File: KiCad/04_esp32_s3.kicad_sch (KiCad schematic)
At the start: 32 parts, among them IC401 ESP32-S3-WROOM-1-N16R8, J401 Conn_01x04_Pin, J402 Conn_01x04_Pin, J403 Conn_01x04_Pin, J404 TF-01A, J405 Conn_01x08_Pin, Q401 SS8050, Q402 SS8050

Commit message: Fix DRC
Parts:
- removed J405: Conn_01x08_Pin, Connector_PinHeader_2.54mm:PinHeader_1x08_P2.54mm_Vertical, symbol Connector:Conn_01x08_Pin
- added J405: Conn_01x06_Pin, Connector_PinHeader_2.54mm:PinHeader_1x06_P2.54mm_Vertical, symbol Connector:Conn_01x06_Pin
- added R414: 0R, Resistor_SMD:R_0805_2012Metric, symbol Device:R
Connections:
- net +3V3: now also J405.3 (Pin_3)
- net +3V3_PER: now also J405.5 (Pin_5)
- net +5V: now also J405.1 (Pin_1)
- net GND: now also J405.2 (Pin_2), J405.4 (Pin_4), J405.6 (Pin_6)
- net at U401.8 (BLK): now also R414.1
- net GPIO2: no longer names the net of IC401.38 (IO2)
- net GPIO47 renamed TFT_BLK
- net TFT_BLK: now also R414.2

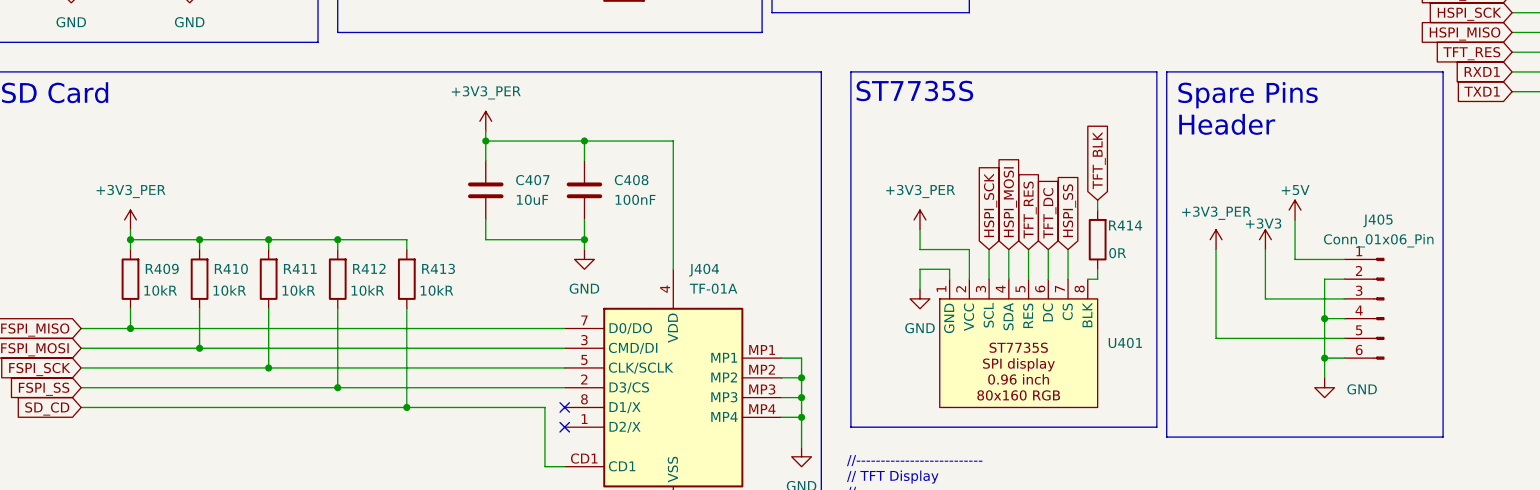
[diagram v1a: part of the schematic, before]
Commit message: Add battery connector and charger
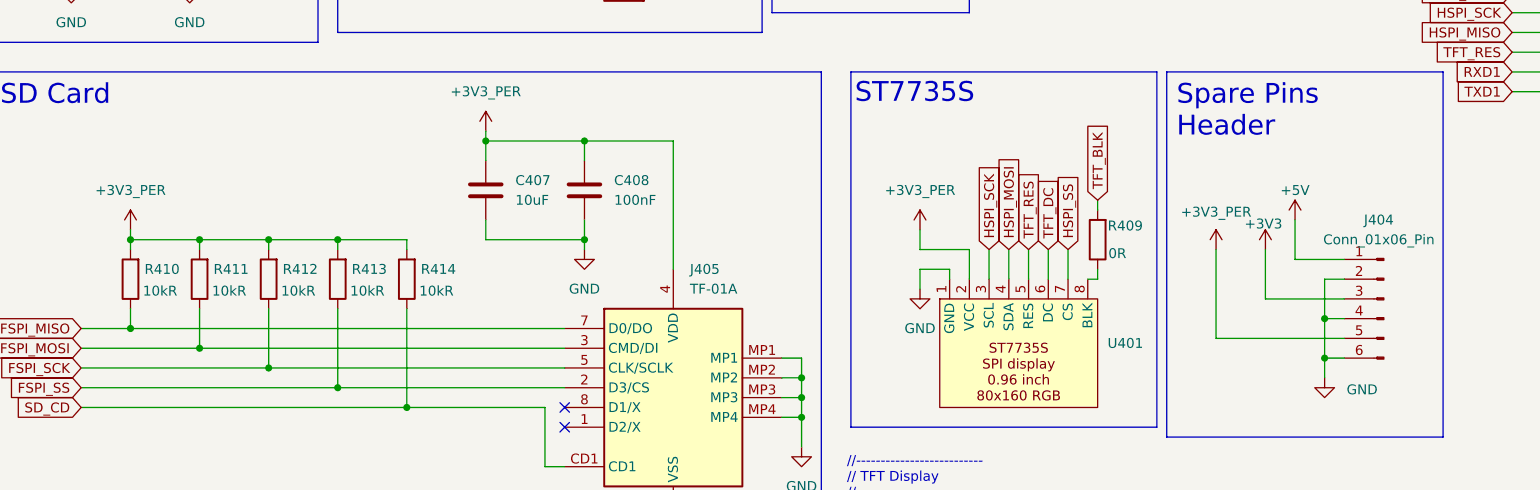
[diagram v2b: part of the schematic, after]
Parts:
- renumbered J405 to J404, J404 to J405, R414 to R409, R409 to R410, R410 to R411, R411 to R412, R412 to R413, R413 to R414
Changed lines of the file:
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@@
 		(on_board yes)
 		(dnp no)
-		(property "Reference" "R413"
+		(property "Reference" "R414"
 			(at 75.184 119.38 0)
 			(effects
@@
 			(project "esp32_s3_weather_webserver"
 				(path "/04e96486-ec4c-4881-a0bf-37cb6ce91c2d/50304ef4-c32e-4a1f-a652-b7b630d07cc6"
-					(reference "R413")
+					(reference "R414")
 					(unit 1)
 				)
@@
 		(dnp no)
 		(fields_autoplaced yes)
-		(property "Reference" "J404"
+		(property "Reference" "J405"
 			(at 107.5533 119.38 0)
 			(effects
@@
 			(project "esp32_s3_weather_webserver"
 				(path "/04e96486-ec4c-4881-a0bf-37cb6ce91c2d/50304ef4-c32e-4a1f-a652-b7b630d07cc6"
-					(reference "J404")
+					(reference "J405")
 					(unit 1)
 				)
@@
 		(on_board yes)
 		(dnp no)
-		(property "Reference" "#PWR0421"
+		(property "Reference" "#PWR0422"
 			(at 181.61 120.65 0)
 			(effects
@@
 			(project "esp32_s3_weather_webserver"
 				(path "/04e96486-ec4c-4881-a0bf-37cb6ce91c2d/50304ef4-c32e-4a1f-a652-b7b630d07cc6"
-					(reference "#PWR0421")
+					(reference "#PWR0422")
 					(unit 1)
 				)
@@
 		(on_board yes)
 		(dnp no)
-		(property "Reference" "#PWR05"
+		(property "Reference" "#PWR0407"
 			(at 123.19 46.99 0)
 			(effects
@@
 			(project "esp32_s3_weather_webserver"
 				(path "/04e96486-ec4c-4881-a0bf-37cb6ce91c2d/50304ef4-c32e-4a1f-a652-b7b630d07cc6"
-					(reference "#PWR05")
+					(reference "#PWR0407")
 					(unit 1)
 				)
@@
 		(on_board yes)
 		(dnp no)
-		(property "Reference" "R412"
+		(property "Reference" "R413"
 			(at 66.294 119.38 0)
 			(effects
@@
 			(project "esp32_s3_weather_webserver"
 				(path "/04e96486-ec4c-4881-a0bf-37cb6ce91c2d/50304ef4-c32e-4a1f-a652-b7b630d07cc6"
-					(reference "R412")
+					(reference "R413")
 					(unit 1)
 				)
@@
 		(on_board yes)
 		(dnp no)
-		(property "Reference" "J405"
+		(property "Reference" "J404"
 			(at 196.215 113.03 0)
 			(effects
@@
 			(project ""
 				(path "/04e96486-ec4c-4881-a0bf-37cb6ce91c2d/50304ef4-c32e-4a1f-a652-b7b630d07cc6"
-					(reference "J405")
+					(reference "J404")
 					(unit 1)
 				)
@@
 		(on_board yes)
 		(dnp no)
-		(property "Reference" "R411"
+		(property "Reference" "R412"
 			(at 57.404 119.38 0)
 			(effects
@@
 			(project "esp32_s3_weather_webserver"
 				(path "/04e96486-ec4c-4881-a0bf-37cb6ce91c2d/50304ef4-c32e-4a1f-a652-b7b630d07cc6"
-					(reference "R411")
+					(reference "R412")
 					(unit 1)
 				)
@@
 		(on_board yes)
 		(dnp no)
-		(property "Reference" "R414"
+		(property "Reference" "R409"
 			(at 163.576 113.792 0)
 			(effects
@@
 			(project "esp32_s3_weather_webserver"
 				(path "/04e96486-ec4c-4881-a0bf-37cb6ce91c2d/50304ef4-c32e-4a1f-a652-b7b630d07cc6"
-					(reference "R414")
+					(reference "R409")
 					(unit 1)
 				)
@@
 		(on_board yes)
 		(dnp no)
-		(property "Reference" "R409"
+		(property "Reference" "R410"
 			(at 39.624 119.38 0)
 			(effects
@@
 			(project "esp32_s3_weather_webserver"
 				(path "/04e96486-ec4c-4881-a0bf-37cb6ce91c2d/50304ef4-c32e-4a1f-a652-b7b630d07cc6"
-					(reference "R409")
+					(reference "R410")
 					(unit 1)
 				)
@@
 		(on_board yes)
 		(dnp no)
-		(property "Reference" "#PWR0423"
+		(property "Reference" "#PWR0421"
 			(at 175.26 120.65 0)
 			(effects
@@
 			(project "esp32_s3_weather_webserver"
 				(path "/04e96486-ec4c-4881-a0bf-37cb6ce91c2d/50304ef4-c32e-4a1f-a652-b7b630d07cc6"
-					(reference "#PWR0423")
+					(reference "#PWR0421")
 					(unit 1)
 				)
@@
 		(on_board yes)
 		(dnp no)
-		(property "Reference" "R410"
+		(property "Reference" "R411"
 			(at 48.514 119.38 0)
 			(effects
@@
 			(project "esp32_s3_weather_webserver"
 				(path "/04e96486-ec4c-4881-a0bf-37cb6ce91c2d/50304ef4-c32e-4a1f-a652-b7b630d07cc6"
-					(reference "R410")
+					(reference "R411")
 					(unit 1)
 				)
@@
 		(on_board yes)
 		(dnp no)
-		(property "Reference" "#PWR04"
+		(property "Reference" "#PWR0408"
 			(at 153.67 46.99 0)
 			(effects
@@
 			(project "esp32_s3_weather_webserver"
 				(path "/04e96486-ec4c-4881-a0bf-37cb6ce91c2d/50304ef4-c32e-4a1f-a652-b7b630d07cc6"
-					(reference "#PWR04")
+					(reference "#PWR0408")
 					(unit 1)
 				)
@@
 		(dnp no)
 		(fields_autoplaced yes)
-		(property "Reference" "#PWR0422"
+		(property "Reference" "#PWR0423"
 			(at 237.49 123.19 0)
 			(effects
@@
 			(project "esp32_s3_weather_webserver"
 				(path "/04e96486-ec4c-4881-a0bf-37cb6ce91c2d/50304ef4-c32e-4a1f-a652-b7b630d07cc6"
-					(reference "#PWR0422")
+					(reference "#PWR0423")
 					(unit 1)
 				)

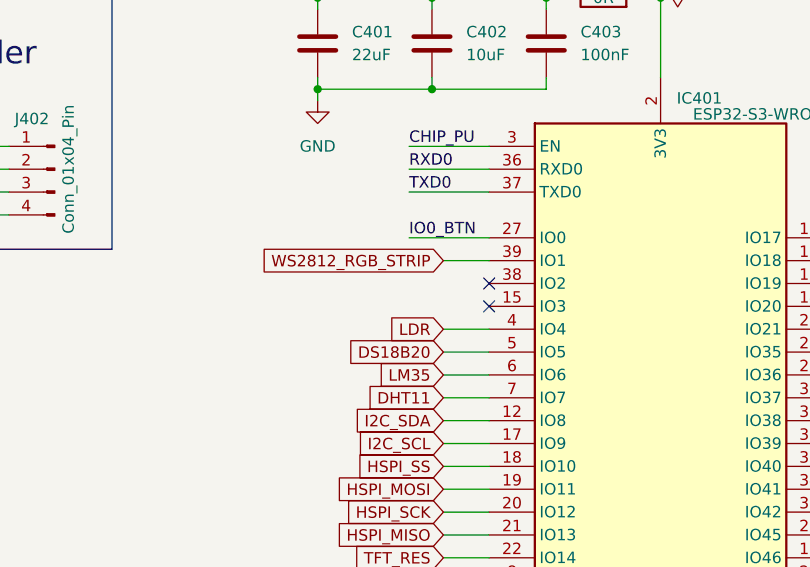
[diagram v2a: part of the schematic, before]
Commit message: Connect VBAT to ADC input to measure battery voltage
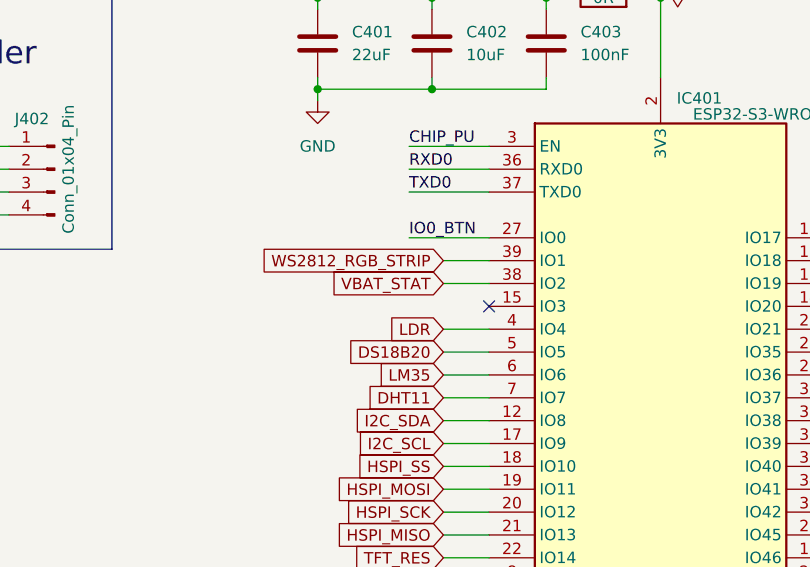
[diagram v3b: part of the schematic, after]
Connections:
- net VBAT_STAT: now reaches IC401.38 (IO2)
- no-connect marks 6 -> 5
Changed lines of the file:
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@@
-	)
-	(no_connect
-		(at 218.44 60.96)
 	)
 	(no_connect
@@
 		(pts
 			(xy 130.81 80.01) (xy 134.62 80.01)
+		)
+		(stroke
+			(width 0)
+			(type default)
+		)
+	)
+	(wire
+		(pts
+			(xy 213.36 60.96) (xy 218.44 60.96)
 		)
 		(stroke
@@
 			(effects
 				(font
+					(size 1.27 1.27)
+				)
+				(justify right)
+				(hide yes)
+			)
+		)
+	)
+	(global_label "VBAT_STAT"
+		(shape input)
+		(at 213.36 60.96 180)
+		(fields_autoplaced yes)
+		(effects
+			(font
+				(size 1.27 1.27)
+			)
+			(justify right)
+		)
+		(property "Intersheetrefs" "${INTERSHEET_REFS}"
+			(at 200.7591 60.96 0)
+			(effects
+				(font

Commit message: Remove broken scheme parts
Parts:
- IC401: Manufacturer_Name Espressif Systems -> (none); Manufacturer_Part_Number ESP32-S3-WROOM-1-N16R8 -> (none); Mouser Part Number 356-ESP32S3WRM1N16R8 -> (none); Mouser Price/Stock https://www.mouser.co.uk/ProductDetail/Espressif-Systems/ES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 -> (none)
- J405: Manufacturer_Name Korean Hroparts Elec -> (none); Manufacturer_Part_Number TF-01A -> (none)
